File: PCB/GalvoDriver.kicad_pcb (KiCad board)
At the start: 4 copper layers, 51.5 x 50 mm, 28 parts, among them J1 Screw_Terminal_01x03, J2 Conn_01x03, J3 Conn_01x06_Male, J4 JUMPER_A, J5 JUMPER_B, J6 AudioJack3, J7 Conn_01x03, U1 TL082, U2 MCP4822, U3 TL082

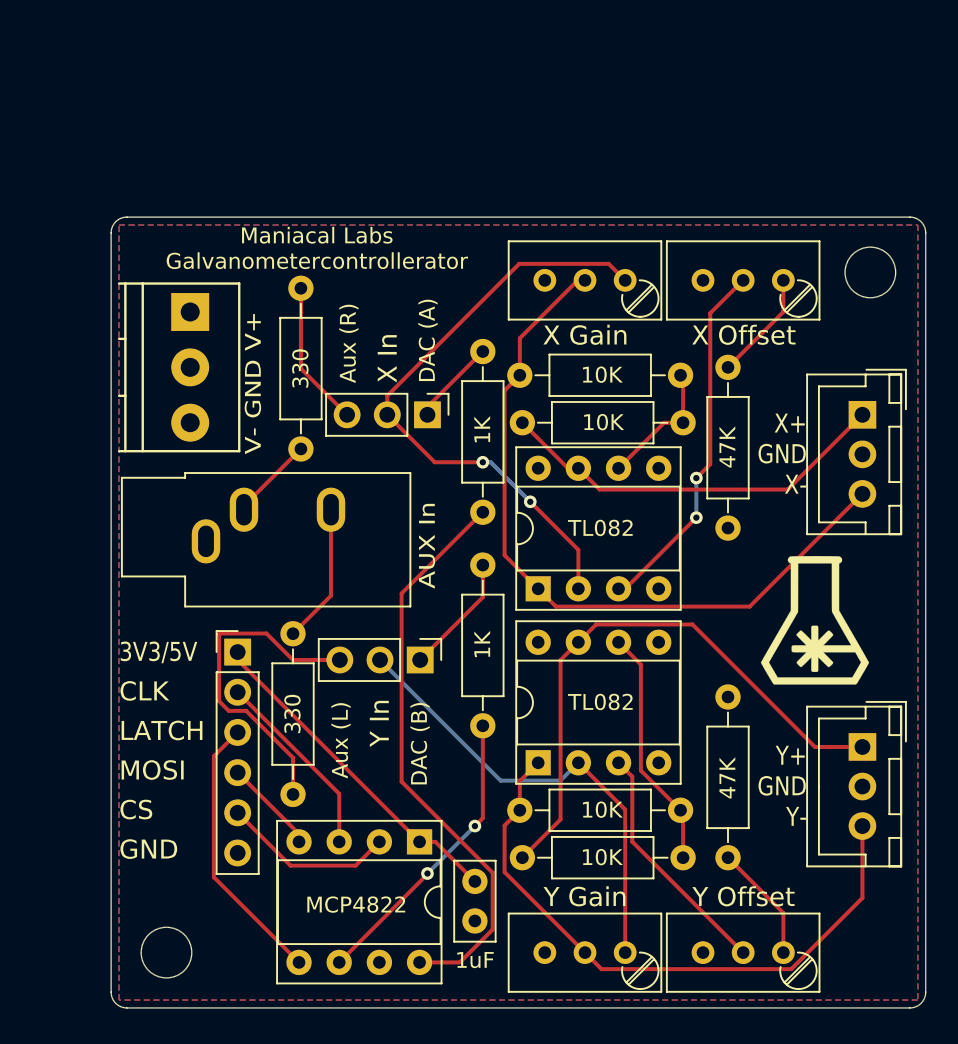
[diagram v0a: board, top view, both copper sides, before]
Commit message: Added Laser Module Control + terminal
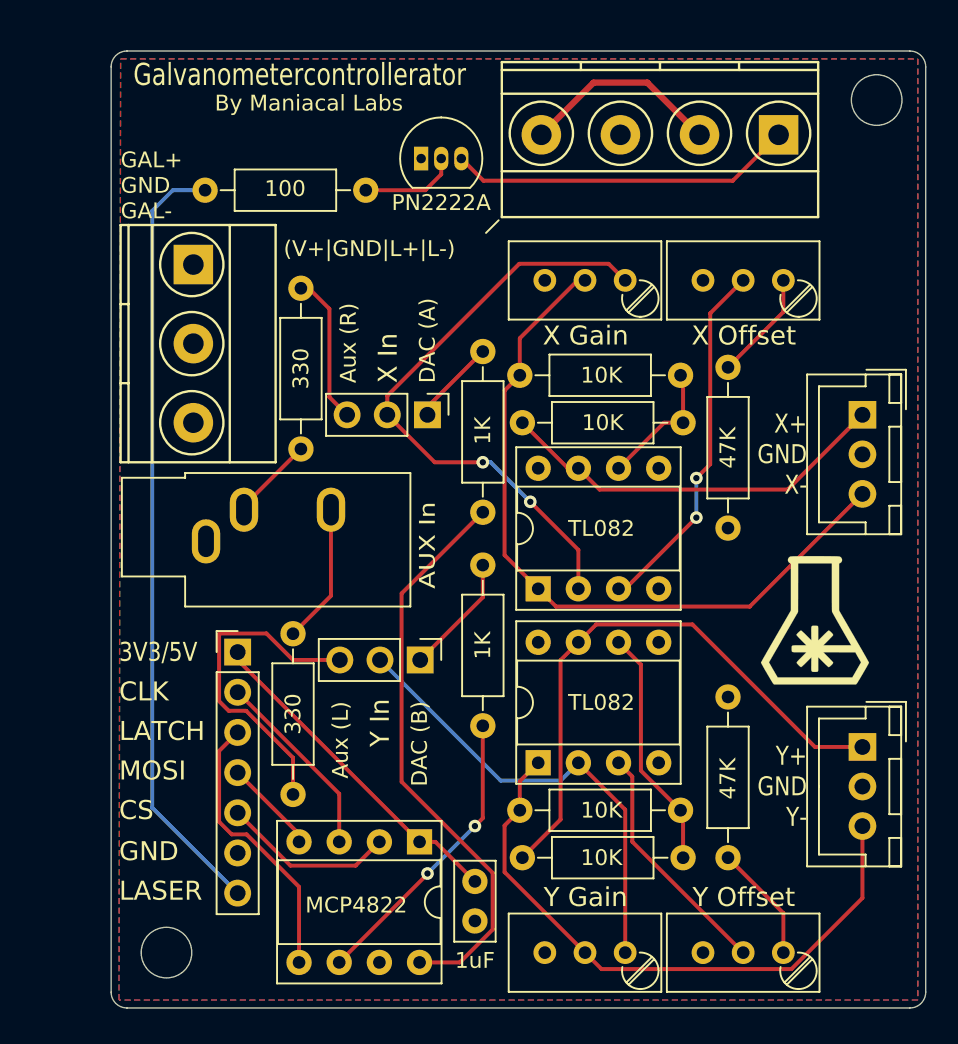
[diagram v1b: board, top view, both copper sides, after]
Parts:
- added J8: Screw_Terminal_01x04, TerminalBlocks_Phoenix:TerminalBlock_Phoenix_MKDS1.5-4pol, F.Cu at (80.2, 41.3)
- added Q1: PN2222A, TO_SOT_Packages_THT:TO-92_Inline_Narrow_Oval, F.Cu at (57.6, 42.8)
- added R11: 100, Resistors_THT:R_Axial_DIN0207_L6.3mm_D2.5mm_P10.16mm_Horizontal, F.Cu at (54.1, 44.8)
- J1: footprint TerminalBlocks_Phoenix:TerminalBlock_Phoenix_PT-3.5mm_3pol -> TerminalBlocks_Phoenix:TerminalBlock_Phoenix_MKDS1.5-3pol
- J3: value Conn_01x06_Male -> Conn_01x07_Male; footprint Pin_Headers:Pin_Header_Straight_1x06_Pitch2.54mm -> Pin_Headers:Pin_Header_Straight_1x07_Pitch2.54mm
- moved REF** 10.9 mm to (86.4, 39.1)
- moved J1 3.01 mm to (43.2, 49.5)
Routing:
- net LASER: track 0.00 -> 49.3 mm
- net Net-(J8-Pad1): track 0.00 -> 21.8 mm
- net VSS: track 0.00 -> 12.7 mm
- net Net-(Q1-Pad2): track 0.00 -> 6.18 mm
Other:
- board size 51.5 x 50 mm -> 51.5 x 60.5 mm
- board text added: "(V+|GND|L+|L-)"
- board text added: "By Maniacal Labs"
- board text added: "GAL+ GND GAL-"
- board text added: "Galvanometercontrollerator"
- board text added: "LASER"
- board text removed: "Maniacal Labs Galvanometercontrollerator"
- board text removed: "V- GND V+"

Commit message: Added terminal labels, exported gerbers for fab.
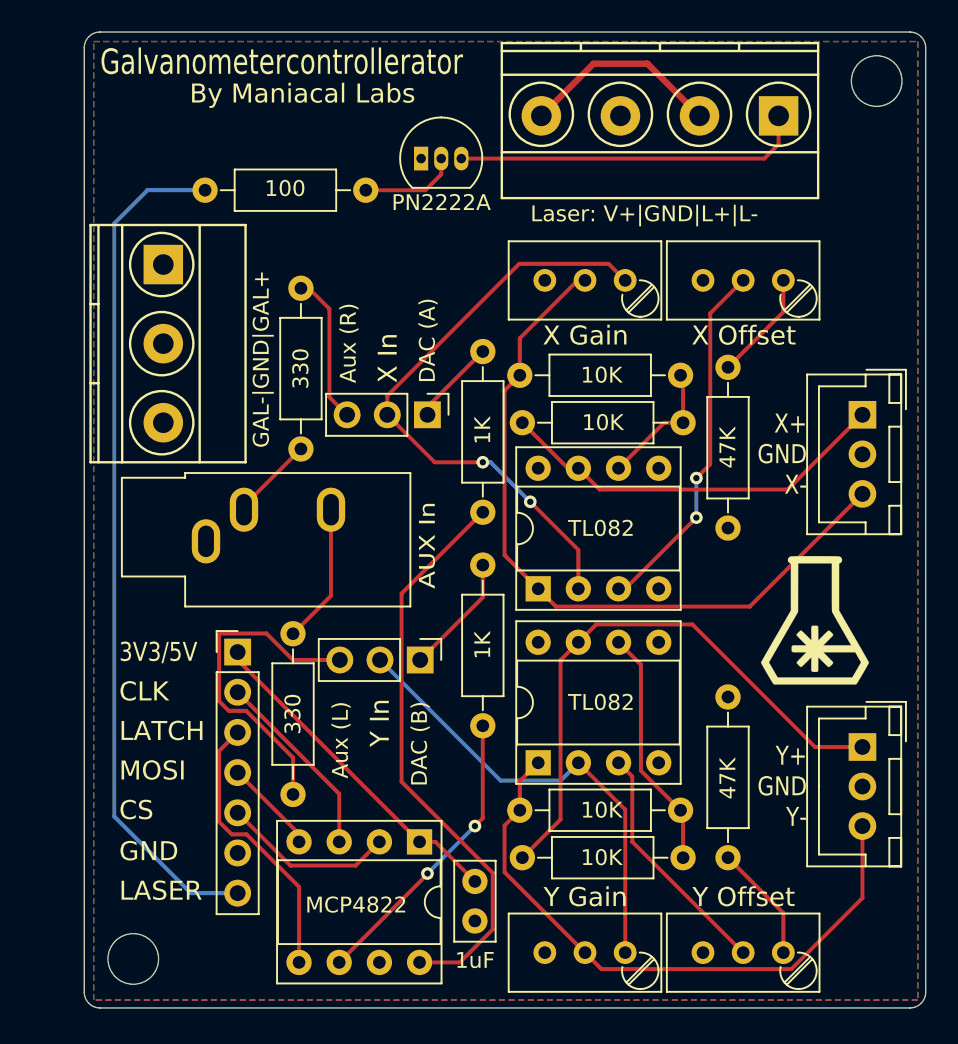
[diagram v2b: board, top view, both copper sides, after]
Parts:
- moved REF** 2.14 mm to (39.4, 93.4)
- moved J1 1.90 mm to (41.3, 49.5)
- moved REF** 1.20 mm to (86.4, 37.9)
- moved J8 1.20 mm to (80.2, 40.1)
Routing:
- net LASER: track 49.3 -> 53.9 mm
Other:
- board size 51.5 x 60.5 mm -> 53.2 x 61.7 mm
- board text added: "GAL-|GND|GAL+"
- board text added: "Laser: V+|GND|L+|L-"
- board text removed: "(V+|GND|L+|L-)"
- board text removed: "GAL+ GND GAL-"

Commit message: Changed decoupling cap value to 0.1uF
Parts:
- C1: value 1uF -> .1uF

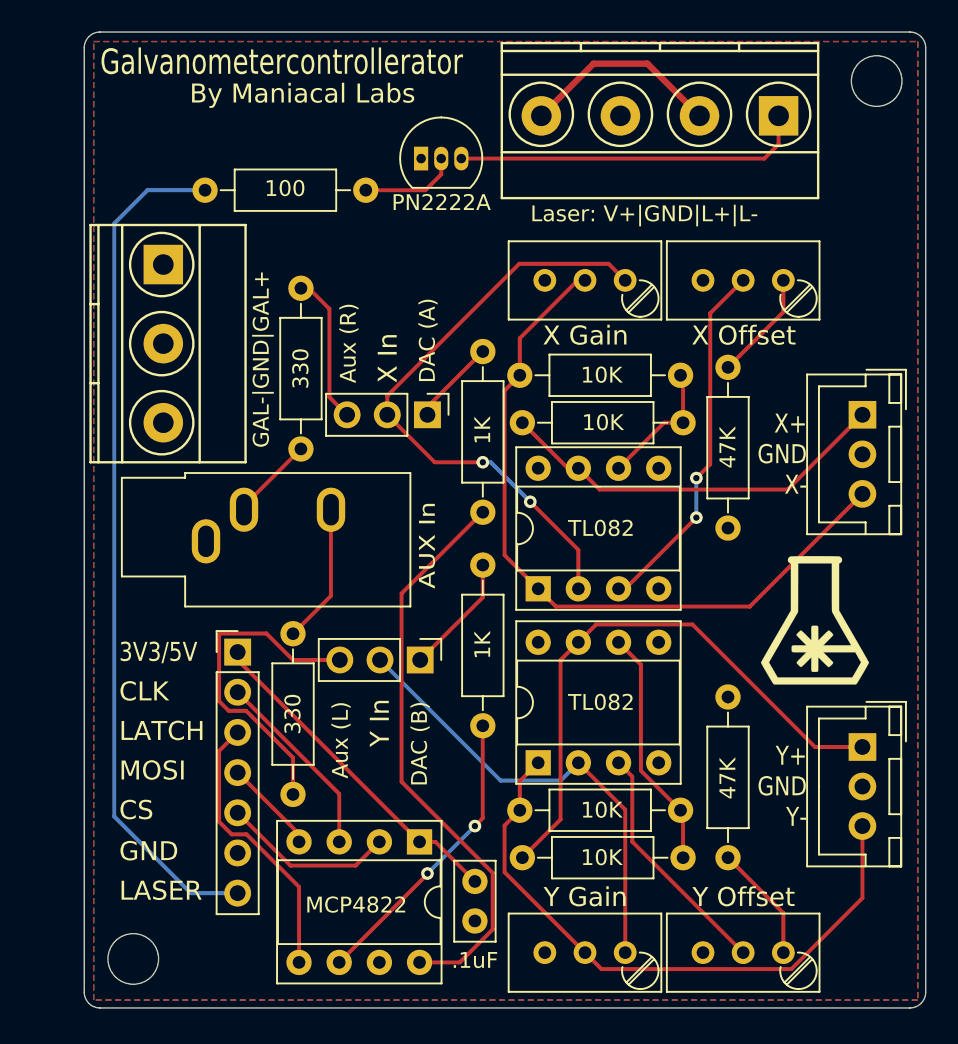
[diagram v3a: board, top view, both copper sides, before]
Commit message: Level shifter, thrm. relief, xistor pad, audio jack move
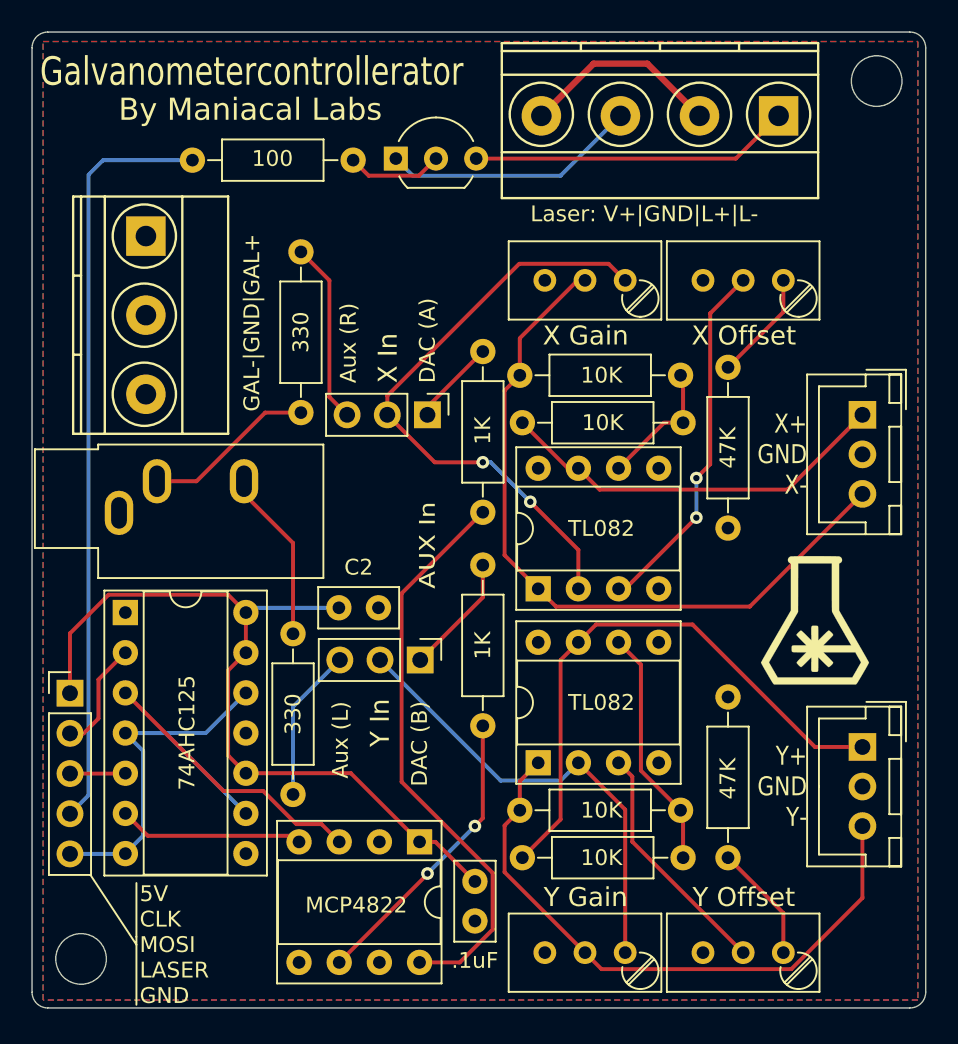
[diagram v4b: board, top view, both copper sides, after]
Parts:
- added C2: .1uF, Capacitors_THT:C_Disc_D5.0mm_W2.5mm_P2.50mm, F.Cu at (52.4, 71.2)
- added U4: 74AHC125, Housings_DIP:DIP-14_W7.62mm_Socket, F.Cu at (38.9, 71.5)
- J3: value Conn_01x07_Male -> Conn_01x05_Male; footprint Pin_Headers:Pin_Header_Straight_1x07_Pitch2.54mm -> Pin_Headers:Pin_Header_Straight_1x05_Pitch2.54mm
- Q1: footprint TO_SOT_Packages_THT:TO-92_Inline_Narrow_Oval -> TO_SOT_Packages_THT:TO-92_Inline_Wide
- moved J3 10.9 mm to (35.4, 76.6)
- moved J6 5.79 mm to (38.5, 65.2)
- moved REF** 3.30 mm to (36.1, 93.4)
- moved R9 2.30 mm to (50.0, 48.7)
- moved J1 2.11 mm to (40.2, 47.7)
- moved R11 2.06 mm to (53.3, 42.9)
- moved Q1 1.60 mm to (56.0, 42.8)
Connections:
- J3 pad 4: Net-(J3-Pad4) -> LASER
- J3 pad 5: Net-(J3-Pad5) -> GND
- U2 pad 2: Net-(J3-Pad5) -> GND
- U2 pad 3: Net-(J3-Pad2) -> CLK
- U2 pad 4: Net-(J3-Pad4) -> MOSI
- U2 pad 5: Net-(J3-Pad3) -> GND
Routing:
- net GND: track 0.00 -> 46.7 mm
- net VDD: track 21.3 -> 50.8 mm
- net CLK: track 0.00 -> 17.4 mm
- net Net-(J3-Pad3): track 17.7 -> 3.51 mm
- net MOSI: track 0.00 -> 11.7 mm
- net Net-(J5-Pad3): track 21.0 -> 9.73 mm
- net Net-(J3-Pad5): track 11.0 -> 0.00 mm
- net LASER: track 53.9 -> 47.8 mm
- net Net-(J3-Pad4): track 5.99 -> 0.00 mm
- net AUDIO_L: track 5.33 -> 10.9 mm
- net Net-(J3-Pad2): track 12.1 -> 7.05 mm
- net AUDIO_R: track 8.83 -> 10.9 mm
- net Net-(J4-Pad3): track 9.50 -> 11.5 mm
- net Net-(J8-Pad1): track 22.2 -> 20.2 mm
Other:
- board size 53.2 x 61.7 mm -> 56.5 x 61.7 mm
- board text added: "5V CLK MOSI LASER GND"
- board text removed: "3V3/5V"
- board text removed: "CLK"
- board text removed: "CS"
- board text removed: "GND"
- board text removed: "LASER"
- board text removed: "LATCH"
- board text removed: "MOSI"
